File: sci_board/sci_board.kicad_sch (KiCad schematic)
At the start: 8 parts

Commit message: propate the changes to RF
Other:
- moved on the sheet: R4
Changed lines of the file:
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@@
 	)
 	(junction
-		(at 104.775 144.78)
-		(diameter 0)
-		(color 0 0 0 0)
-	)
-	(junction
 		(at 142.24 138.43)
 		(diameter 0)
@@
 	(wire
 		(pts
-			(xy 99.06 144.78) (xy 104.775 144.78)
-		)
-		(stroke
-			(width 0)
-			(type default)
-		)
-	)
-	(wire
-		(pts
 			(xy 86.995 118.745) (xy 88.265 118.745)
 		)
@@
 	)
 	(label "ATTN"
-		(at 104.775 152.4 270)
+		(at 117.475 152.4 270)
 		(fields_autoplaced yes)
 		(effects
@@
 	)
 	(symbol
+		(lib_id "power:+3V3")
+		(at 99.06 144.78 0)
+		(unit 1)
+		(exclude_from_sim no)
+		(in_bom yes)
+		(on_board yes)
+		(dnp no)
+		(fields_autoplaced yes)
+		(property "Reference" "#PWR035"
+			(at 99.06 148.59 0)
+			(effects
+				(font
+					(size 1.27 1.27)
+				)
+				(hide yes)
+			)
+		)
+		(property "Value" "+3V3_STM32_Core"
+			(at 99.06 139.7 0)
+			(effects
+				(font
+					(size 1.27 1.27)
+				)
+			)
+		)
+		(property "Footprint" ""
+			(at 99.06 144.78 0)
+			(effects
+				(font
+					(size 1.27 1.27)
+				)
+				(hide yes)
+			)
+		)
+		(property "Datasheet" ""
+			(at 99.06 144.78 0)
+			(effects
+				(font
+					(size 1.27 1.27)
+				)
+				(hide yes)
+			)
+		)
+		(property "Description" "Power symbol creates a global label with name \"+3V3\""
+			(at 99.06 144.78 0)
+			(effects
+				(font
+					(size 1.27 1.27)
+				)
+				(hide yes)
+			)
+		)
+		(pin "1"
+		)
+		(instances
+			(project "sci_board"
+				(path "/b4b2c88d-f6cd-4e60-862d-e21f68728580"
+					(reference "#PWR035")
+					(unit 1)
+				)
+			)
+		)
+	)
+	(symbol
 		(lib_id "power:PWR_FLAG")
 		(at 46.99 20.32 270)
@@
 	(symbol
 		(lib_id "Device:R")
-		(at 104.775 148.59 0)
+		(at 117.475 148.59 0)
 		(unit 1)
 		(exclude_from_sim no)
@@
 		(dnp no)
 		(property "Reference" "R4"
-			(at 102.87 158.75 0)
+			(at 115.57 158.75 0)
 			(effects
 				(font
@@
 		)
 		(property "Value" "330K"
-			(at 102.87 161.29 0)
+			(at 115.57 161.29 0)
 			(effects
 				(font
@@
 		)
 		(property "Footprint" "Resistor_SMD:R_0402_1005Metric_Pad0.72x0.64mm_HandSolder"
-			(at 102.997 148.59 90)
+			(at 115.697 148.59 90)
 			(effects
 				(font
@@
 		)
 		(property "Datasheet" "https://www.yageo.com/upload/media/product/products/datasheet/rchip/PYu-RC_Group_51_RoHS_L_12.pdf"
-			(at 104.775 148.59 0)
+			(at 117.475 148.59 0)
 			(effects
 				(font
@@
 		)
 		(property "Description" "Resistor"
-			(at 104.775 148.59 0)
+			(at 117.475 148.59 0)
 			(effects
 				(font
@@
 		)
 		(property "Manufacturer" "YAGEO"
-			(at 104.775 148.59 0)
+			(at 117.475 148.59 0)
 			(effects
 				(font
@@
 		)
 		(property "Note" "generic pullup/down"
-			(at 104.775 148.59 0)
+			(at 117.475 148.59 0)
 			(effects
 				(font
@@
 		)
 		(property "Part Number" "RC0402FR-07100KL"
-			(at 104.775 148.59 0)
+			(at 117.475 148.59 0)
 			(effects
 				(font
@@
 		)
 		(property "Tolerance" "1"
-			(at 104.775 148.59 0)
+			(at 117.475 148.59 0)
 			(effects
 				(font
@@
 	(symbol
 		(lib_id "power:+3V3")
-		(at 104.775 144.78 0)
+		(at 117.475 144.78 0)
 		(unit 1)
 		(exclude_from_sim no)
@@
 		(fields_autoplaced yes)
 		(property "Reference" "#PWR027"
-			(at 104.775 148.59 0)
+			(at 117.475 148.59 0)
 			(effects
 				(font
@@
 		)
 		(property "Value" "+3V3_STM32_Core"
-			(at 104.775 139.7 0)
+			(at 117.475 139.7 0)
 			(effects
 				(font
@@
 		)
 		(property "Footprint" ""
-			(at 104.775 144.78 0)
+			(at 117.475 144.78 0)
 			(effects
 				(font
@@
 		)
 		(property "Datasheet" ""
-			(at 104.775 144.78 0)
+			(at 117.475 144.78 0)
 			(effects
 				(font
@@
 		)
 		(property "Description" "Power symbol creates a global label with name \"+3V3\""
-			(at 104.775 144.78 0)
+			(at 117.475 144.78 0)
 			(effects
 				(font

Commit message: tweaks before merge
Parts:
- H1, H2, H3, H4: footprint Project:MountingHole_4.3mm_M4_Pad_Via_Custom -> Common:MountingHole_4.3mm_M4_Pad_Via_Custom

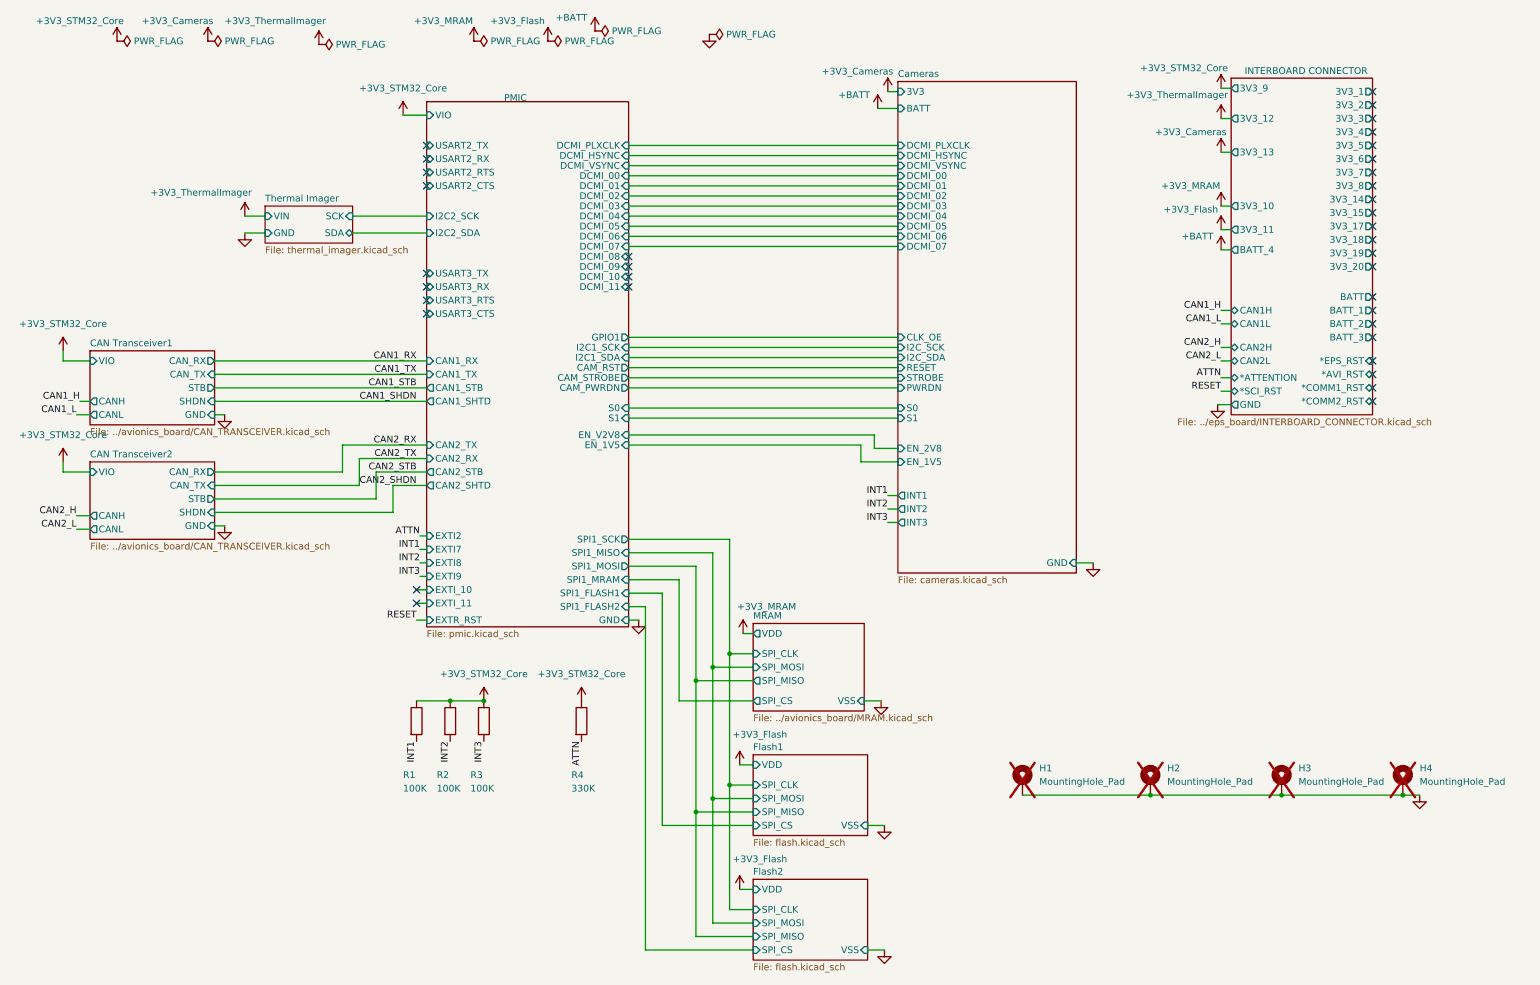
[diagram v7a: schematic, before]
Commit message: local switches and monitors for SCI and RF
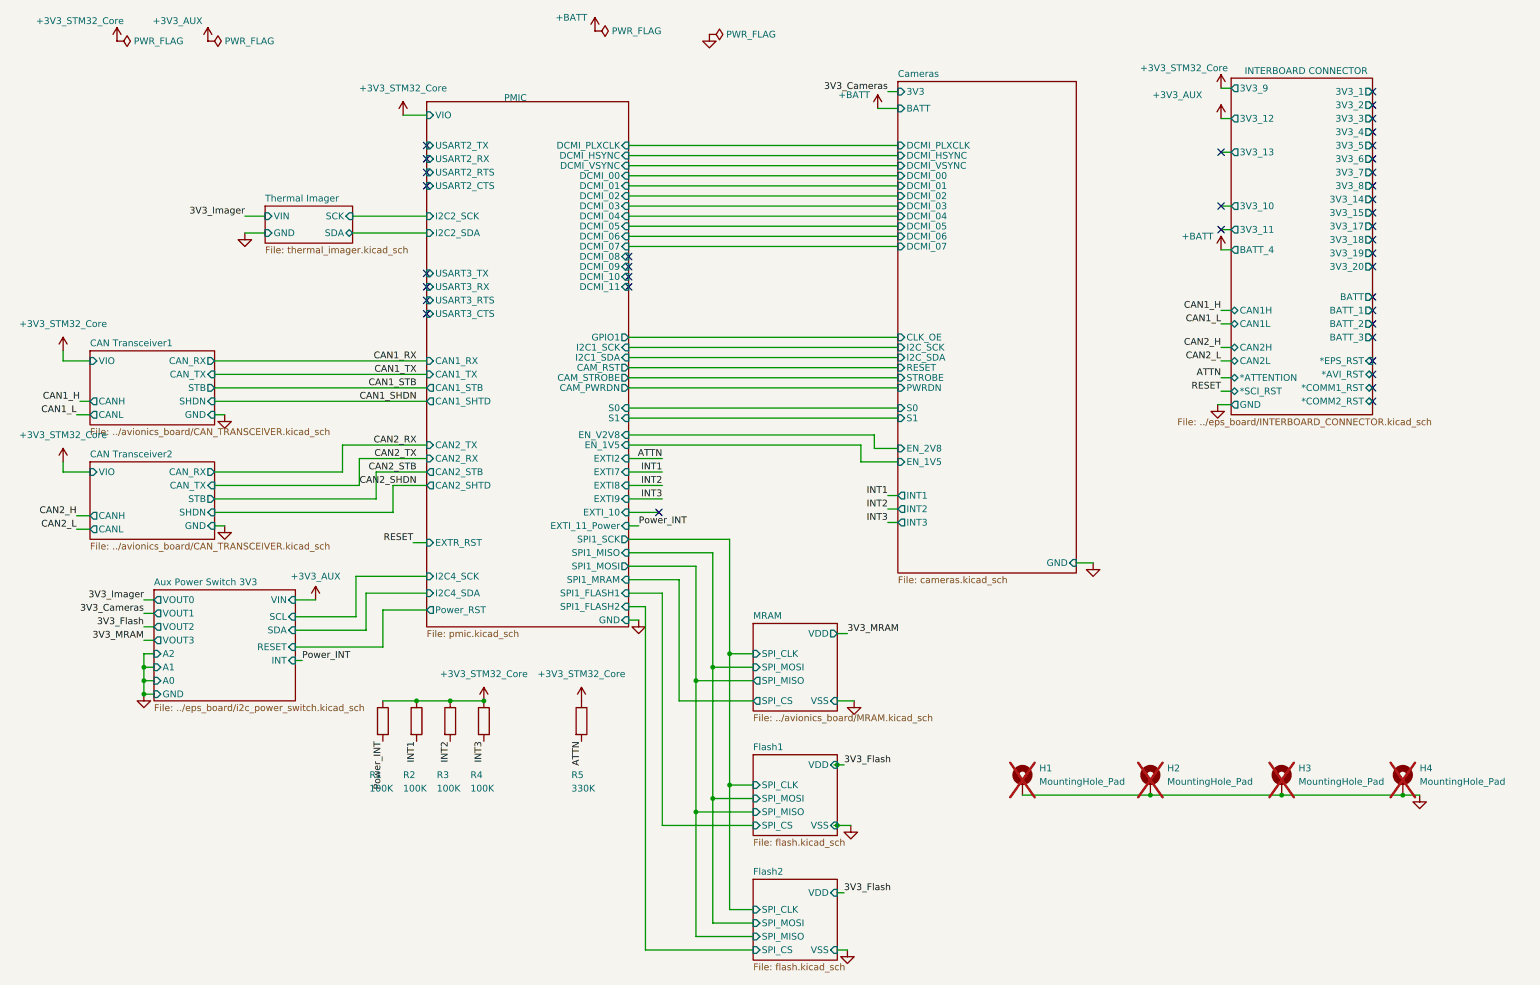
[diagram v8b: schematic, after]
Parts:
- added R1: 100K, Resistor_SMD:R_0402_1005Metric_Pad0.72x0.64mm_HandSolder, symbol Device:R
- renumbered R1 to R2, R2 to R3, R3 to R4, R4 to R5
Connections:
- net +3V3_STM32_Core: now also R1.1
- new net Power_INT: R1.2
- no-connect marks 36 -> 38
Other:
- added sheet Aux Power Switch 3V3 (../eps_board/i2c_power_switch.kicad_sch)
- sheet PMIC ports: added EXTI_11_Power, I2C4_SCK, I2C4_SDA, Power_RST; removed EXTI_11
